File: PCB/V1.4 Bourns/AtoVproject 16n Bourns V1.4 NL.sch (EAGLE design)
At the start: 161 parts, among them IC1 NCS2007, IC10 TEENSY_3.2_PIN, IC2 NCS2007, IC3 NCS2007, IC4 NCS2007, IC5 MCP6004_SMD, IC6 MCP6004_SMD, IC7 MCP6004_SMD, IC8 MCP6004_SMD, IC9 CD74HC4067SM96, J1 THONKICONN, J10 THONKICONN, J11 THONKICONN, J12 THONKICONN, J13 THONKICONN, J14 THONKICONN, J15 THONKICONN, J16 THONKICONN, J2 THONKICONN, J3 THONKICONN, J4 THONKICONN, J5 THONKICONN, J6 THONKICONN, J7 THONKICONN, J8 THONKICONN, J9 THONKICONN

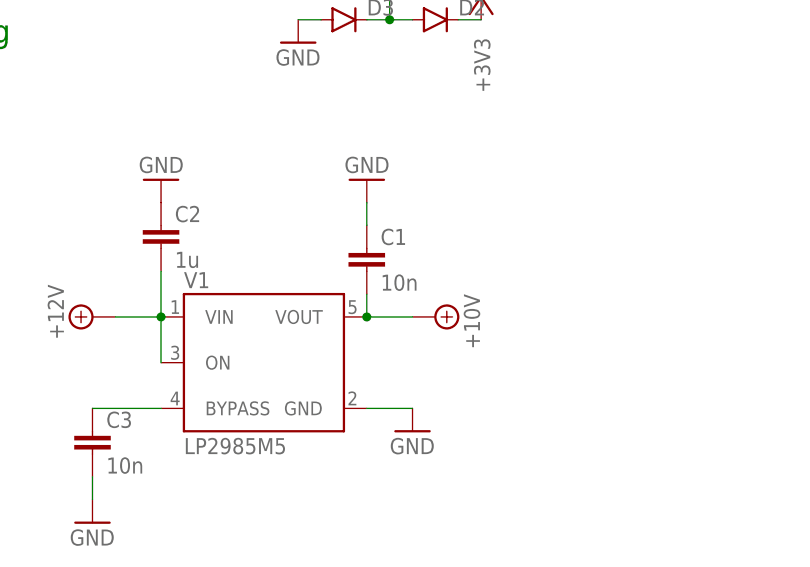
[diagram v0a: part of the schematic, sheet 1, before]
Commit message: Fix C1 Value in eagle files
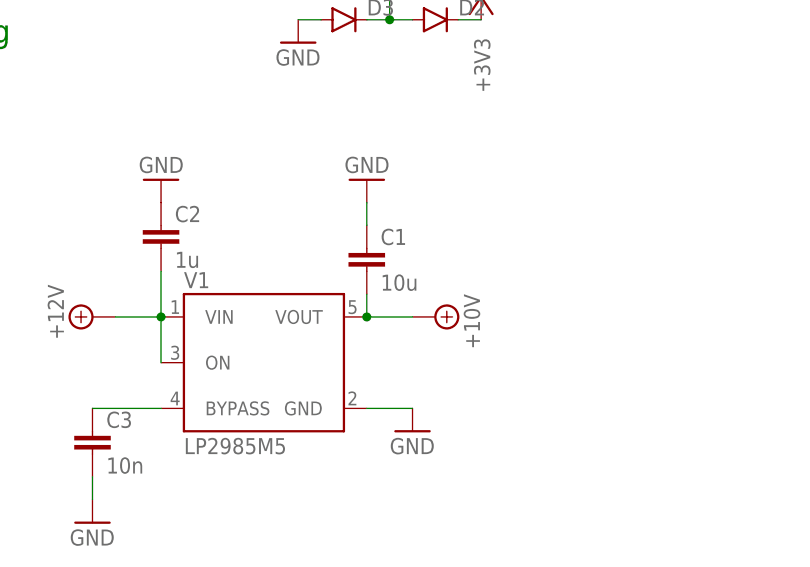
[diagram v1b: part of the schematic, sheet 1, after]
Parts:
- C1: value 10n -> 10u
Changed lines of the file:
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@@
 <?xml version="1.0" encoding="utf-8"?>
 <!DOCTYPE eagle SYSTEM "eagle.dtd">
-<eagle version="9.5.0">
+<eagle version="9.5.2">
 <drawing>
 <settings>
@@
 <part name="C3" library="rcl" library_urn="urn:adsk.eagle:library:334" deviceset="C-EU" device="C0805" package3d_urn="urn:adsk.eagle:package:23617/2" value="10n"/>
 <part name="C2" library="rcl" library_urn="urn:adsk.eagle:library:334" deviceset="C-EU" device="C0805" package3d_urn="urn:adsk.eagle:package:23617/2" value="1u"/>
-<part name="C1" library="rcl" library_urn="urn:adsk.eagle:library:334" deviceset="C-EU" device="C0805" package3d_urn="urn:adsk.eagle:package:23617/2" value="10n"/>
+<part name="C1" library="rcl" library_urn="urn:adsk.eagle:library:334" deviceset="C-EU" device="C0805" package3d_urn="urn:adsk.eagle:package:23617/2" value="10u"/>
 <part name="SUPPLY69" library="supply2" library_urn="urn:adsk.eagle:library:372" deviceset="+5V" device=""/>
 <part name="GND26" library="supply1" deviceset="GND" device=""/>
